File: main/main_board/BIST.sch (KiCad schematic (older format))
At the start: 0 parts

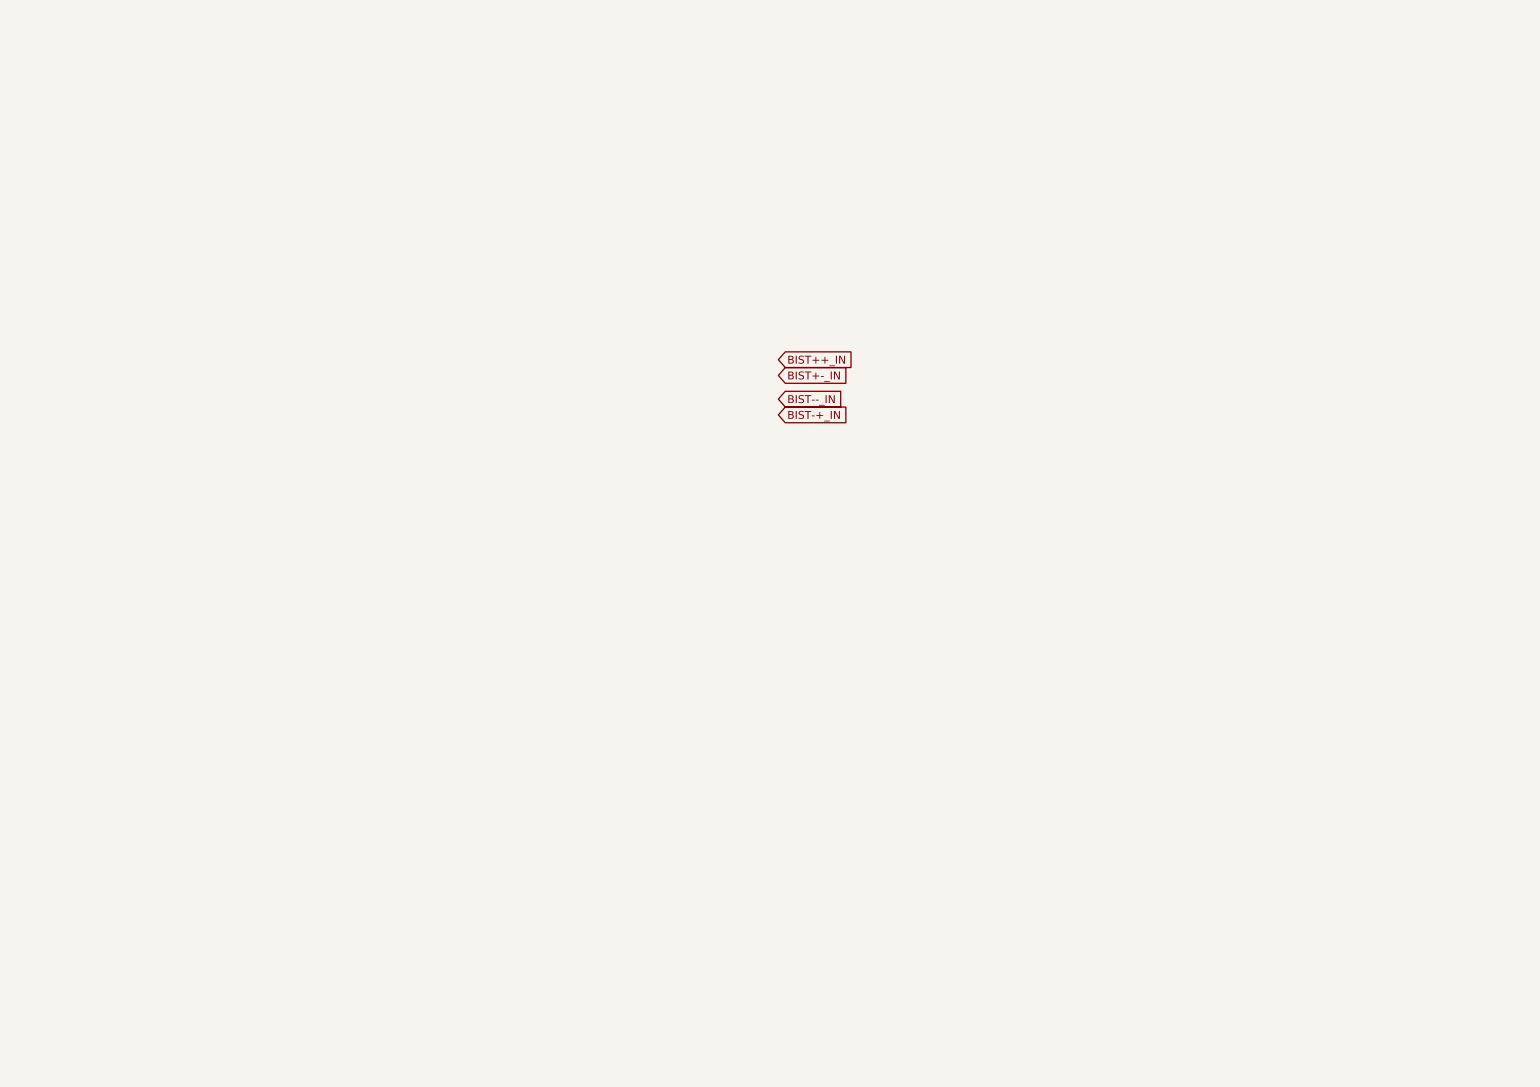
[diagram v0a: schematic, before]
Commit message: Mechanical feature layout on main board (edge connector and mount hole locations).  Added some dimension callouts to the input board. Tweaked grounding on main board schematic.  Chassis ground is not connected to main board ground except via an optional capacitor.  Chassis ground comes in on the power connector. Added BIST DAC, including additions to power.sch and input_slots.sch.
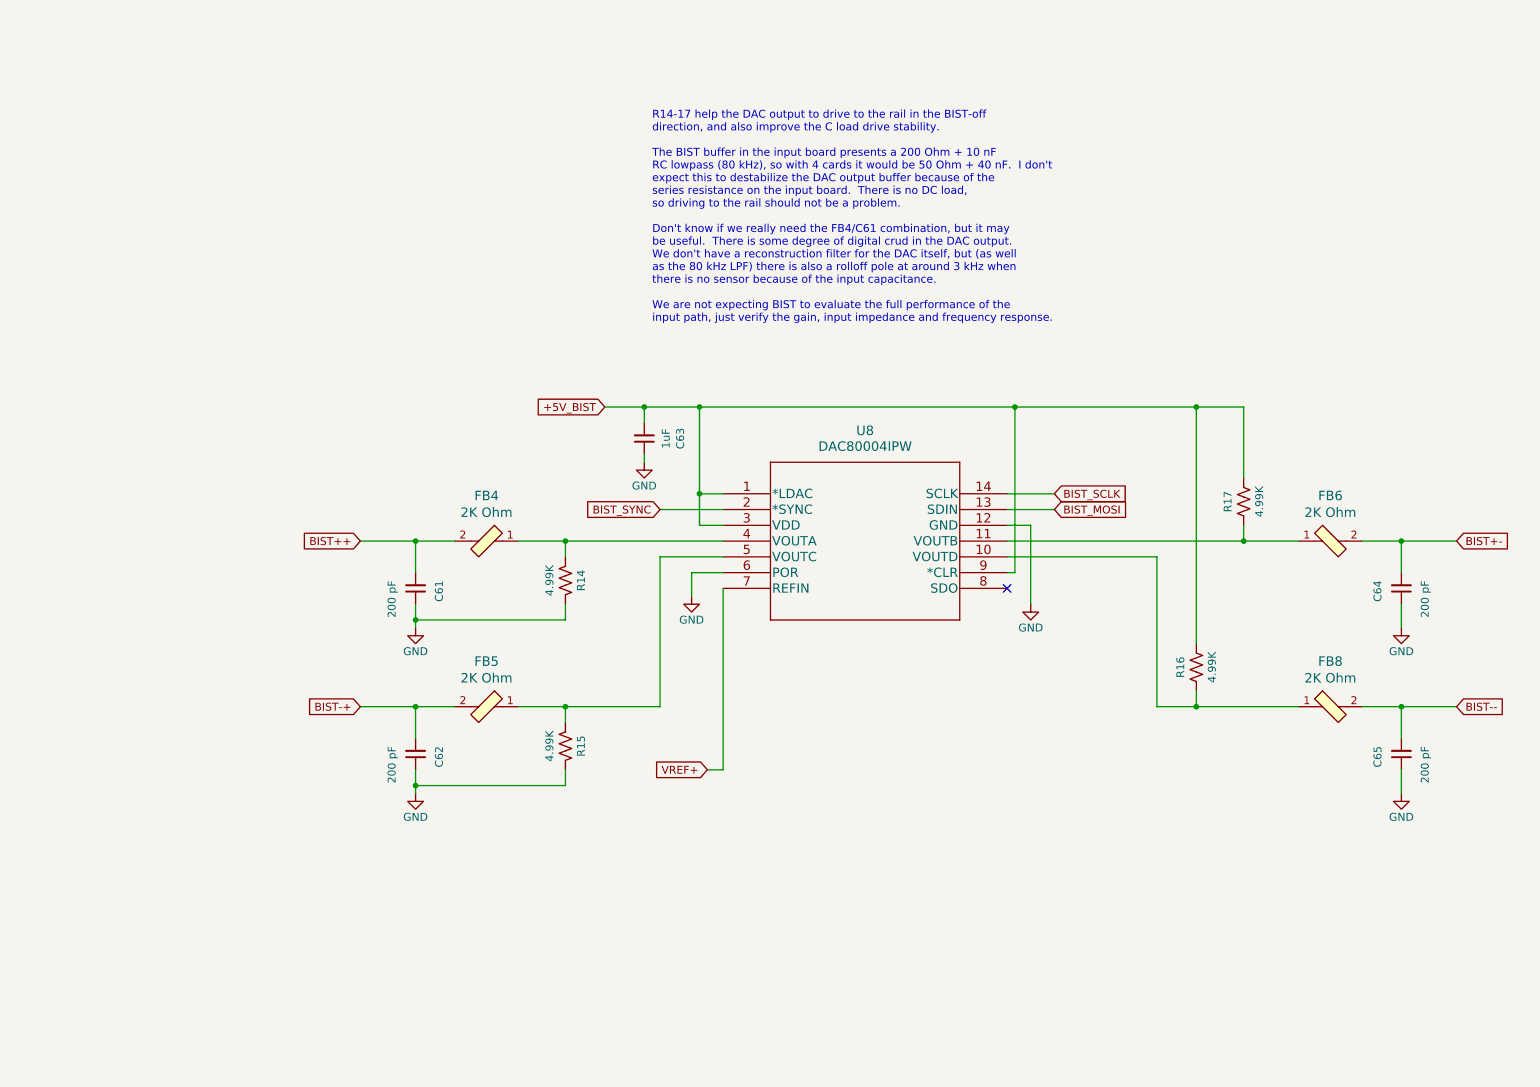
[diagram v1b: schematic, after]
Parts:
- added C61, C62, C64, C65: 200 pF, Capacitor_SMD:C_0603_1608Metric, symbol Device:C_Small
- added C63: 1uF, Capacitor_SMD:C_0805_2012Metric, symbol Device:C_Small
- added FB4, FB5, FB6, FB8: 2K Ohm, Inductor_SMD:L_0805_2012Metric, symbol dk_Ferrite-Beads-and-Chips:MPZ2012S601AT000
- added R14, R15, R16, R17: 4.99K, Resistor_SMD:R_0603_1608Metric, symbol Device:R_US
- added U8: DAC80004IPW, Package_SO:SSOP-14_5.3x6.2mm_P0.65mm, symbol DAC80004IPW:DAC80004IPW
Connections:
- new net: FB8.1, R16.1, U8.10 (VOUTD)
- new net: FB6.1, R17.1, U8.11 (VOUTB)
- new net: FB4.1, R14.2, U8.4 (VOUTA)
- new net: FB5.1, R15.2, U8.5 (VOUTC)
- new net +5V_BIST: C63.2, R16.2, R17.2, U8.1 (*LDAC), U8.3 (VDD), U8.9 (*CLR)
- new net BIST++: C61.2, FB4.2
- new net BIST+-: C64.2, FB6.2
- new net BIST-+: C62.2, FB5.2
- new net BIST--: C65.2, FB8.2
- new net BIST_MOSI: U8.13 (SDIN)
- new net BIST_SCLK: U8.14 (SCLK)
- new net BIST_SYNC: U8.2 (*SYNC)
- new net GND: C61.1, C62.1, C63.1, C64.1, C65.1, R14.1, R15.1, U8.12 (GND), U8.6 (POR)
- new net VREF+: U8.7 (REFIN)
- no-connect marks 0 -> 1
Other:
- note added: "R14-17 help the DAC output to drive to the rail in the BIST-off\ndirection, and also improve the C load drive stability. \n\nThe BIST buffer in the input board presents a 200 Ohm + 10 nF\nRC lowpass (80 kHz), so with 4 cards it would be 50 Ohm + 40 nF. I don't\nexpect this to destabilize the DAC output buffer because of the\nseries resistance on the input board. There is no DC load,\nso driving t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"

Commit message: Changes related to pin mapping. There's a new BIST unit in the Microzed symbol, and the unit ordering has changed. I also added SDI lines to the input slots which could be used to configure the ADC in a future version of the input board. Added some wire labels for easier routing.
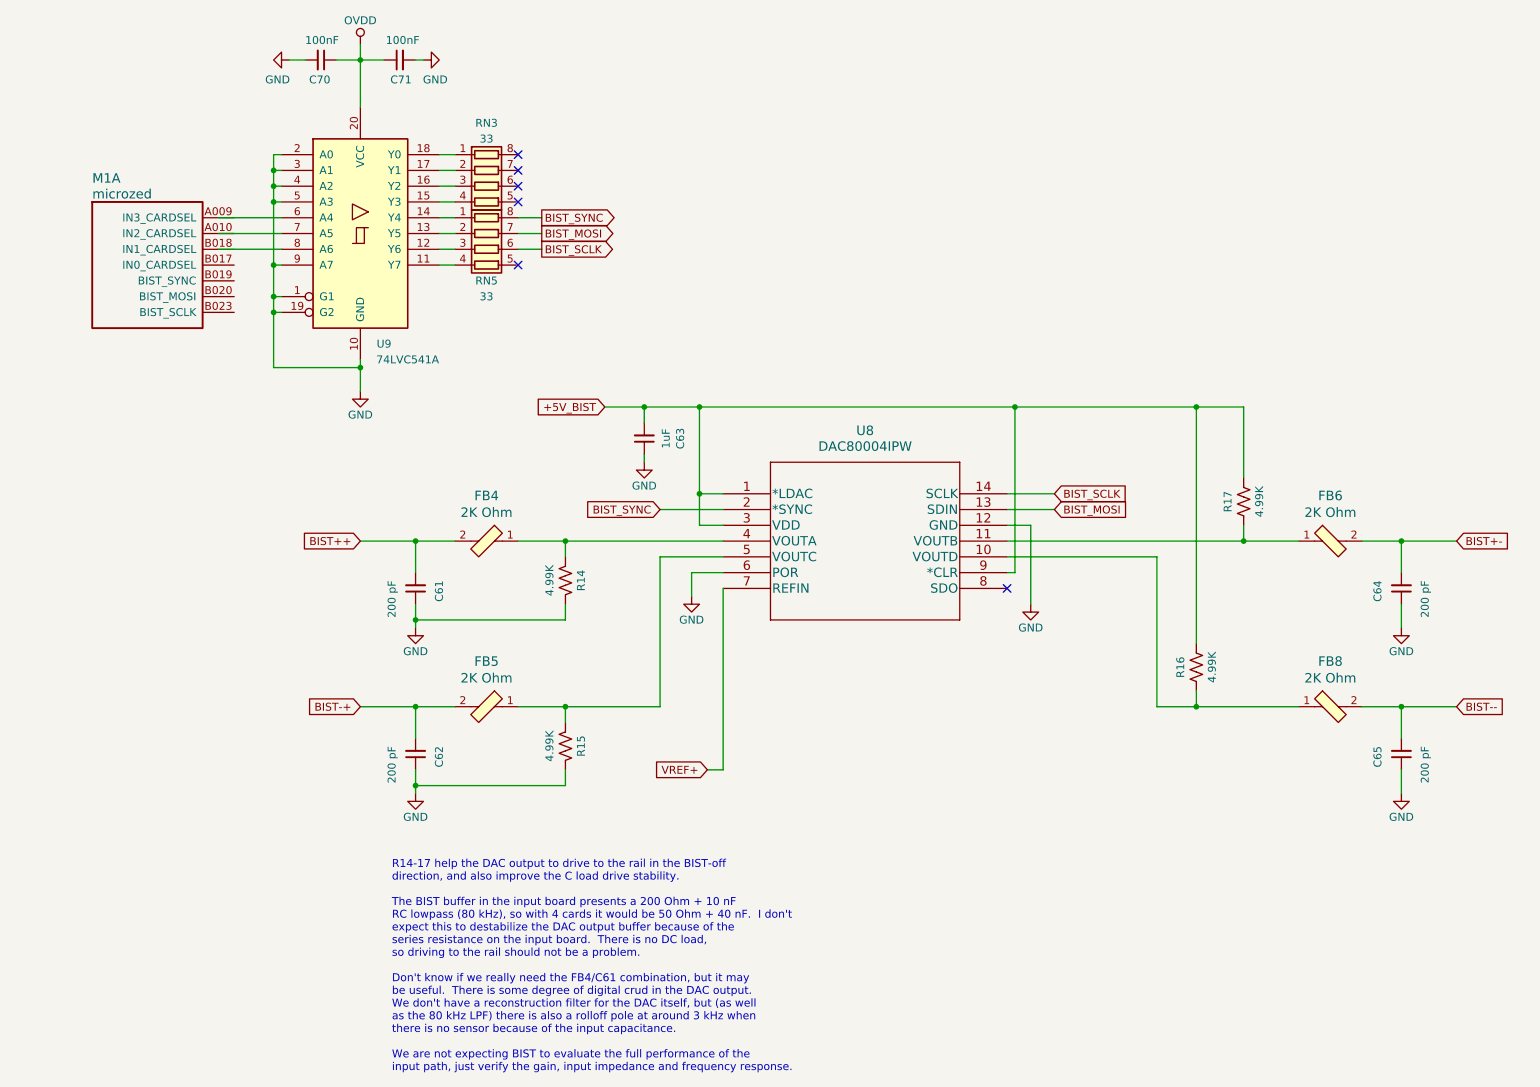
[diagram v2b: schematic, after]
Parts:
- added C70, C71: 100nF, Capacitor_SMD:C_0603_1608Metric, symbol Device:C_Small
- added M1: microzed, main_board:Microzed, symbol microzed:microzed
- added RN3, RN5: 33, Resistor_SMD:R_Array_Convex_4x0603, symbol Device:R_Pack04
- added U9: 74LVC541A, input:my-SSOP-20_5.3x7.2mm_P0.65mm, symbol 74xx:74LS541
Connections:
- net labels added: OVDD
- wire segments 62 -> 99
- no-connect marks 1 -> 6

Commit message: Various preparations for routing the main board. Cleaned up the BOM and reconciled it with the Digikey BOM, so lots of component attributes have changed. This involved pinning down some components which had been vague, especially ferrite beads and chip capacitors. 1uF capacitors have all been changed to 10uF. Changed CARDSEL lines to be buffered rather than filtered, since we had the unused buffers sitting there. Another pass on the Microzed pin mapping.  Brought out the DEBUG LVDS line, and tweaked orderings. Added RC filter and pullups on I2C and PROBE_CONFIG.  We might need level translators here to get >=3.3V Added mount holes for the low volt regulator daughtercard, and dimensioned the connector location.
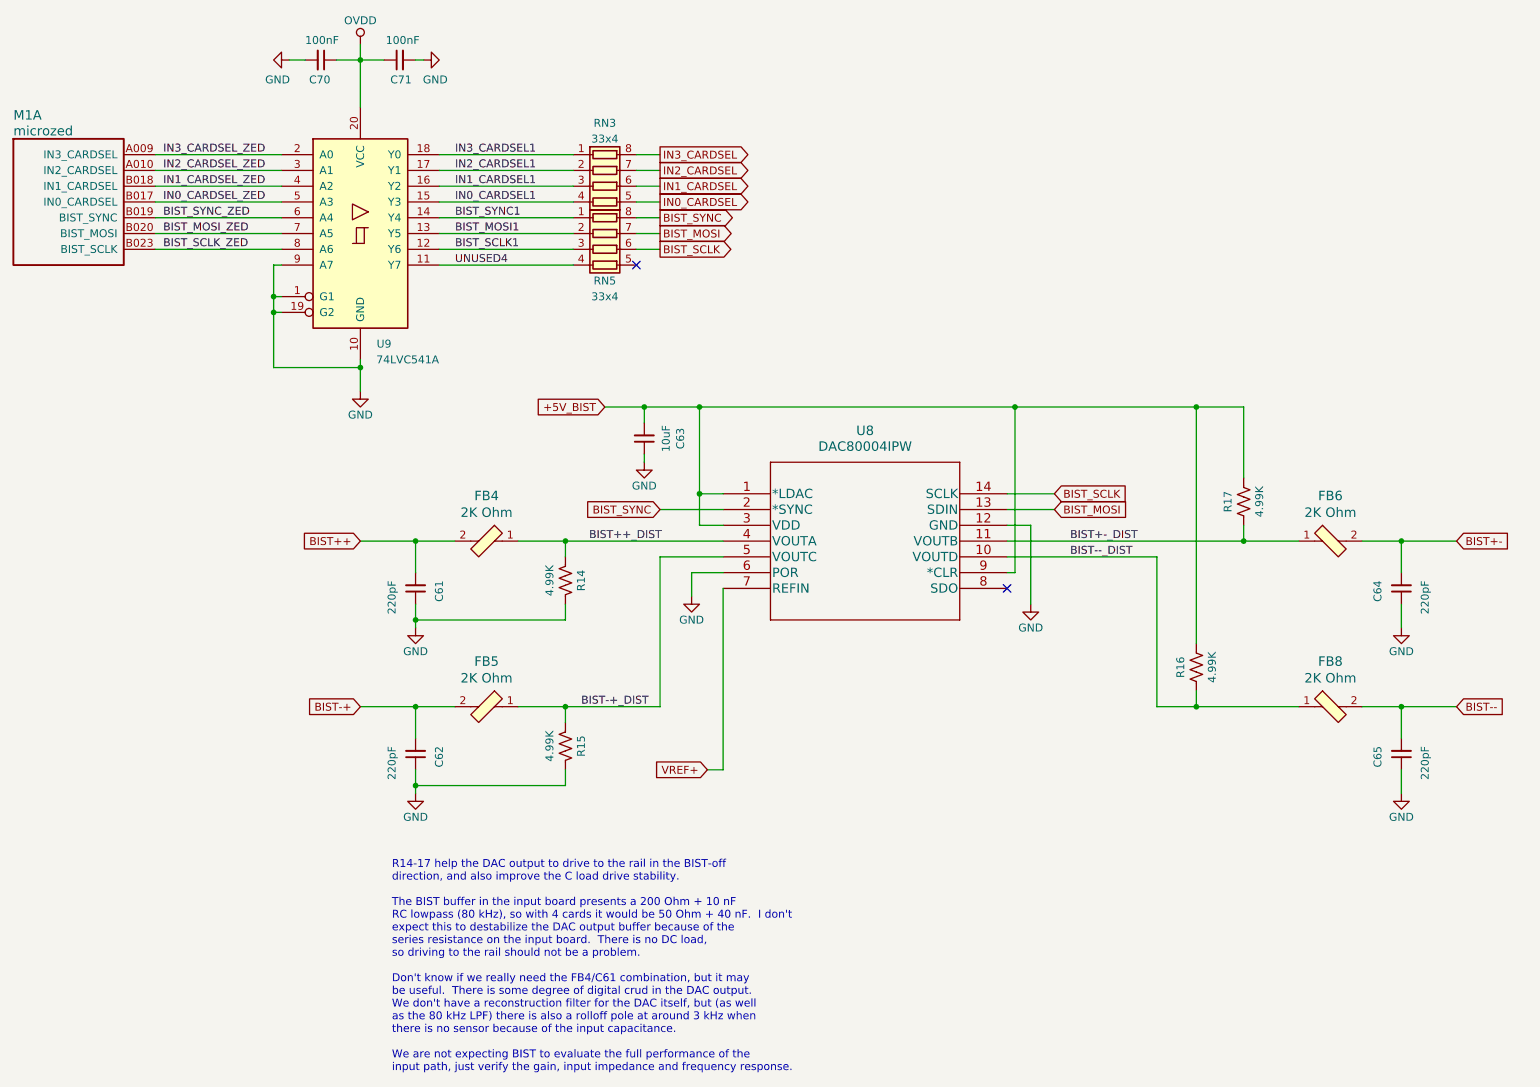
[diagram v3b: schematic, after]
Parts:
- C61, C62, C64, C65: value 200 pF -> 220pF; DK line (none) -> 15; Description (none) -> CAP CER 220PF 50V C0G/NP0 0603; Digikey (none) -> 1276-1048-1-ND; MPN (none) -> CL10C221JB8NNNC; Manufacturer (none) -> Samsung Electro-Mechanics
- C63: value 1uF -> 10uF; footprint Capacitor_SMD:C_0805_2012Metric -> Capacitor_SMD:C_0603_1608Metric; DK line 27 -> 20; Description CAP CER 1UF 16V X7R 0805 -> CAP CER 10UF 6.3V X5R 0603; Digikey 1276-6471-1-ND -> 478-5318-1-ND; MPN CL21B105KOFNNNG -> 06036D106MAT2A; Manufacturer (none) -> AVX
- C70, C71: DK line 2 -> 18; MPN (none) -> CC0603KRX7R8BB104; Manufacturer (none) -> Yageo
- FB4, FB5, FB6, FB8: Category Filters -> (none); DK line 5 -> 16; DK_Datasheet_Link https://product.tdk.com/info/en/catalog/datasheets/beads_co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 -> (none); DK_Detail_Page /product-detail/en/tdk-corporation/MPZ2012S601AT000/445-220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 -> (none); Digi-Key_PN 240-2396-1-ND -> (none); Status Active -> (none)
- R14, R15, R16, R17: DK line (none) -> 34; Description (none) -> RES 4.99K OHM 1% 1/8W 0603; Digikey (none) -> RNCP0603FTD4K99CT-ND; MPN (none) -> RNCP0603FTD4K99; Manufacturer (none) -> Stackpole Electronics Inc
- RN3, RN5: value 33 -> 33x4; DK line 13 -> 25; MPN (none) -> CAY16-330J4LF; Manufacturer (none) -> Bourns Inc.
- U8: DK line (none) -> 8; Description (none) -> IC DAC 16BIT V-OUT 14TSSOP; Digikey (none) -> 296-44598-5-ND; MPN (none) -> DAC80004IPW; Manufacturer (none) -> Texas Instruments
- U9: DK line 11 -> 17; MPN (none) -> SN74LVC541ADBR; Manufacturer (none) -> Texas Instruments
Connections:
- net labels added: BIST++_DIST, BIST+-_DIST, BIST-+_DIST, BIST--_DIST, BIST_MOSI1, BIST_MOSI_ZED, BIST_SCLK1, BIST_SCLK_ZED, BIST_SYNC1, BIST_SYNC_ZED, IN0_CARDSEL, IN0_CARDSEL1, IN0_CARDSEL_ZED, IN1_CARDSEL, IN1_CARDSEL1, IN1_CARDSEL_ZED, IN2_CARDSEL, IN2_CARDSEL1, IN2_CARDSEL_ZED, IN3_CARDSEL, IN3_CARDSEL1, IN3_CARDSEL_ZED, UNUSED4
- no-connect marks 6 -> 2
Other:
- moved on the sheet: M1A, RN3, RN5
